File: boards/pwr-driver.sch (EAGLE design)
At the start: 32 parts

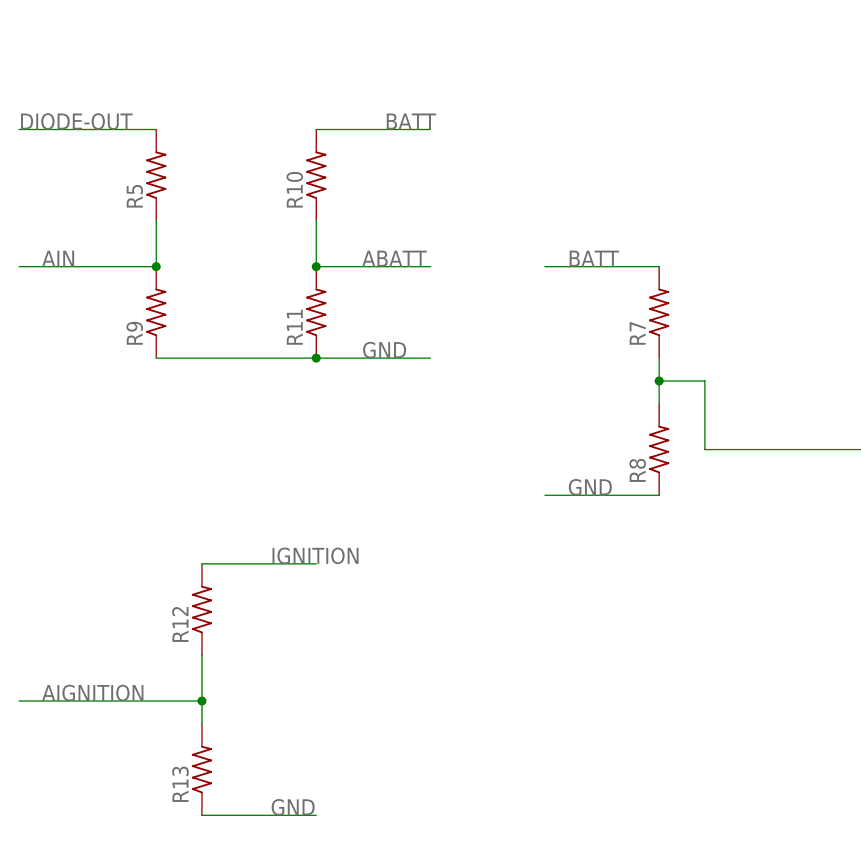
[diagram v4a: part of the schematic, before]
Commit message: Added resistor values to all of the resistor dividors.
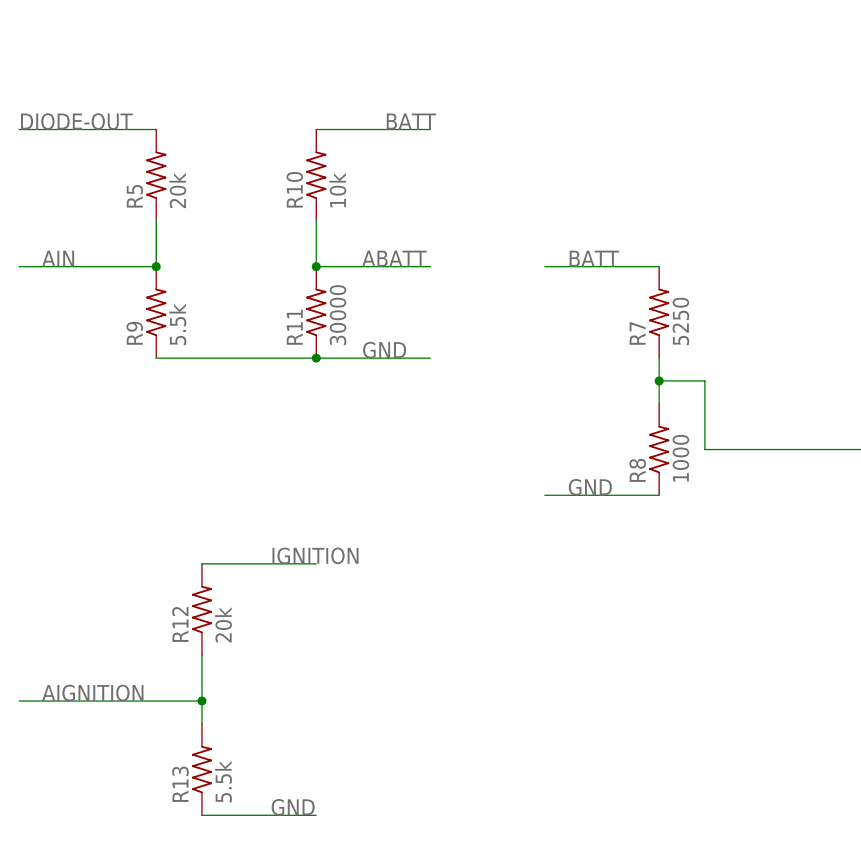
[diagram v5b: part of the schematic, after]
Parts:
- R10: value (none) -> 10k
- R11: value (none) -> 30000
- R12, R5: value (none) -> 20k
- R13, R9: value (none) -> 5.5k
- R7: value (none) -> 5250
- R8: value (none) -> 1000
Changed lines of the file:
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@@
 <part name="C5" library="resistor" deviceset="C-US" device="C0603" value=".1uf"/>
 <part name="U$1" library="needed-parts" deviceset="MPM80" device=""/>
-<part name="R7" library="resistor" deviceset="R-US_" device="R0603"/>
-<part name="R8" library="resistor" deviceset="R-US_" device="R0603"/>
+<part name="R7" library="resistor" deviceset="R-US_" device="R0603" value="5250"/>
+<part name="R8" library="resistor" deviceset="R-US_" device="R0603" value="1000"/>
 <part name="U$3" library="needed-parts" deviceset="STEP-UP-FROM-AMAZON" device=""/>
 <part name="BATT" library="pinhead" deviceset="PINHD-1X2" device=""/>
@@
 <part name="U$8" library="needed-parts" deviceset="PTC" device=""/>
 <part name="U$10" library="needed-parts" deviceset="ADS1013" device=""/>
-<part name="R5" library="resistor" deviceset="R-US_" device="R0603"/>
-<part name="R9" library="resistor" deviceset="R-US_" device="R0603"/>
-<part name="R10" library="resistor" deviceset="R-US_" device="R0603"/>
-<part name="R11" library="resistor" deviceset="R-US_" device="R0603"/>
-<part name="R12" library="resistor" deviceset="R-US_" device="R0603"/>
-<part name="R13" library="resistor" deviceset="R-US_" device="R0603"/>
+<part name="R5" library="resistor" deviceset="R-US_" device="R0603" value="20k"/>
+<part name="R9" library="resistor" deviceset="R-US_" device="R0603" value="5.5k"/>
+<part name="R10" library="resistor" deviceset="R-US_" device="R0603" value="10k"/>
+<part name="R11" library="resistor" deviceset="R-US_" device="R0603" value="30000"/>
+<part name="R12" library="resistor" deviceset="R-US_" device="R0603" value="20k"/>
+<part name="R13" library="resistor" deviceset="R-US_" device="R0603" value="5.5k"/>
 <part name="C2" library="resistor" deviceset="C-US" device="C0603" value=".1uf"/>
 <part name="U$15" library="needed-parts" deviceset="DIODE-403" device=""/>

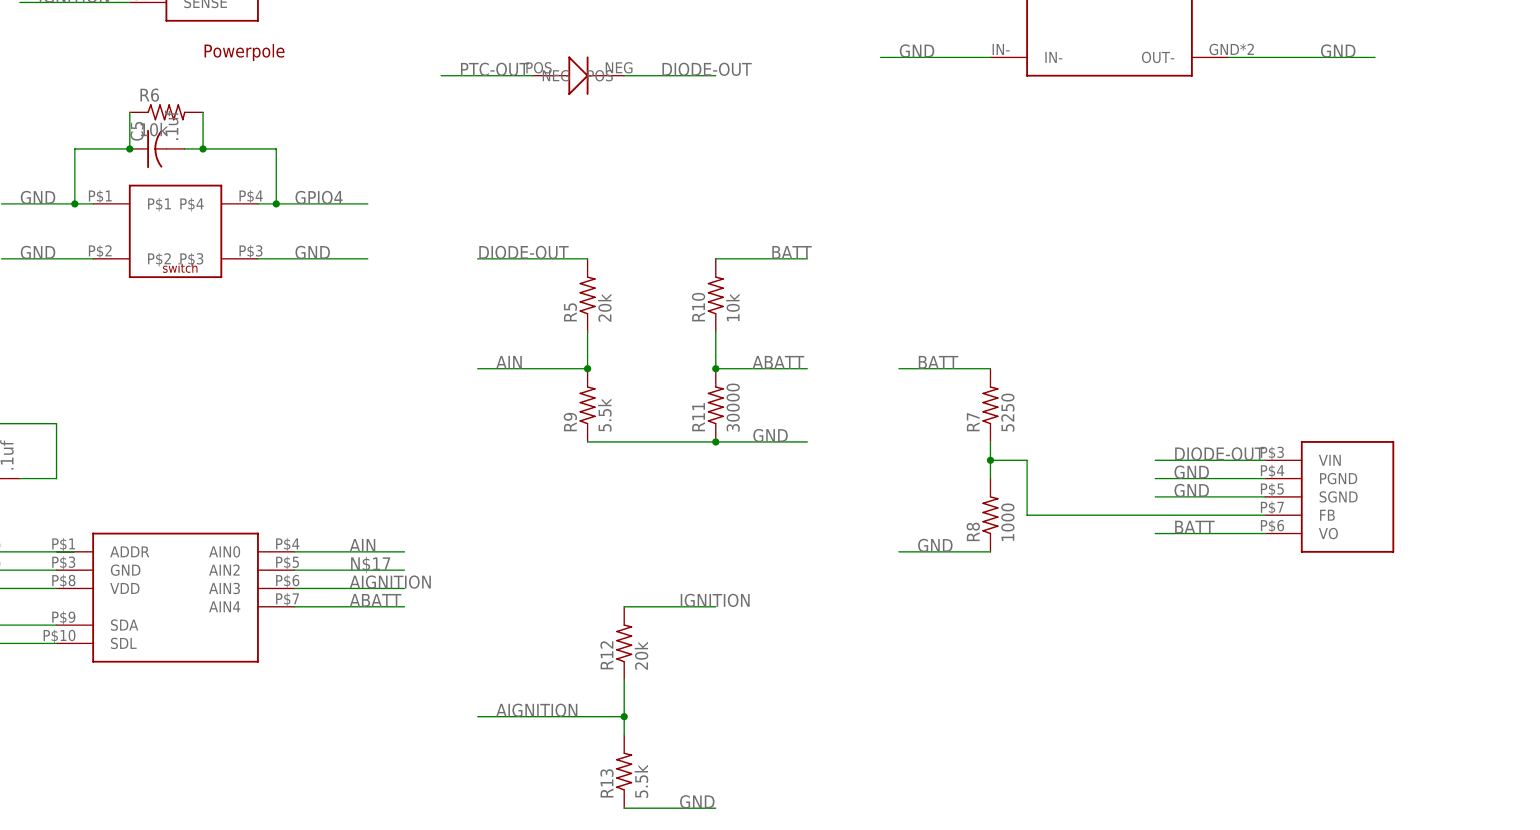
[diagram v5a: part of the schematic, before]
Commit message: dding description of Resistor dividors to schematic.
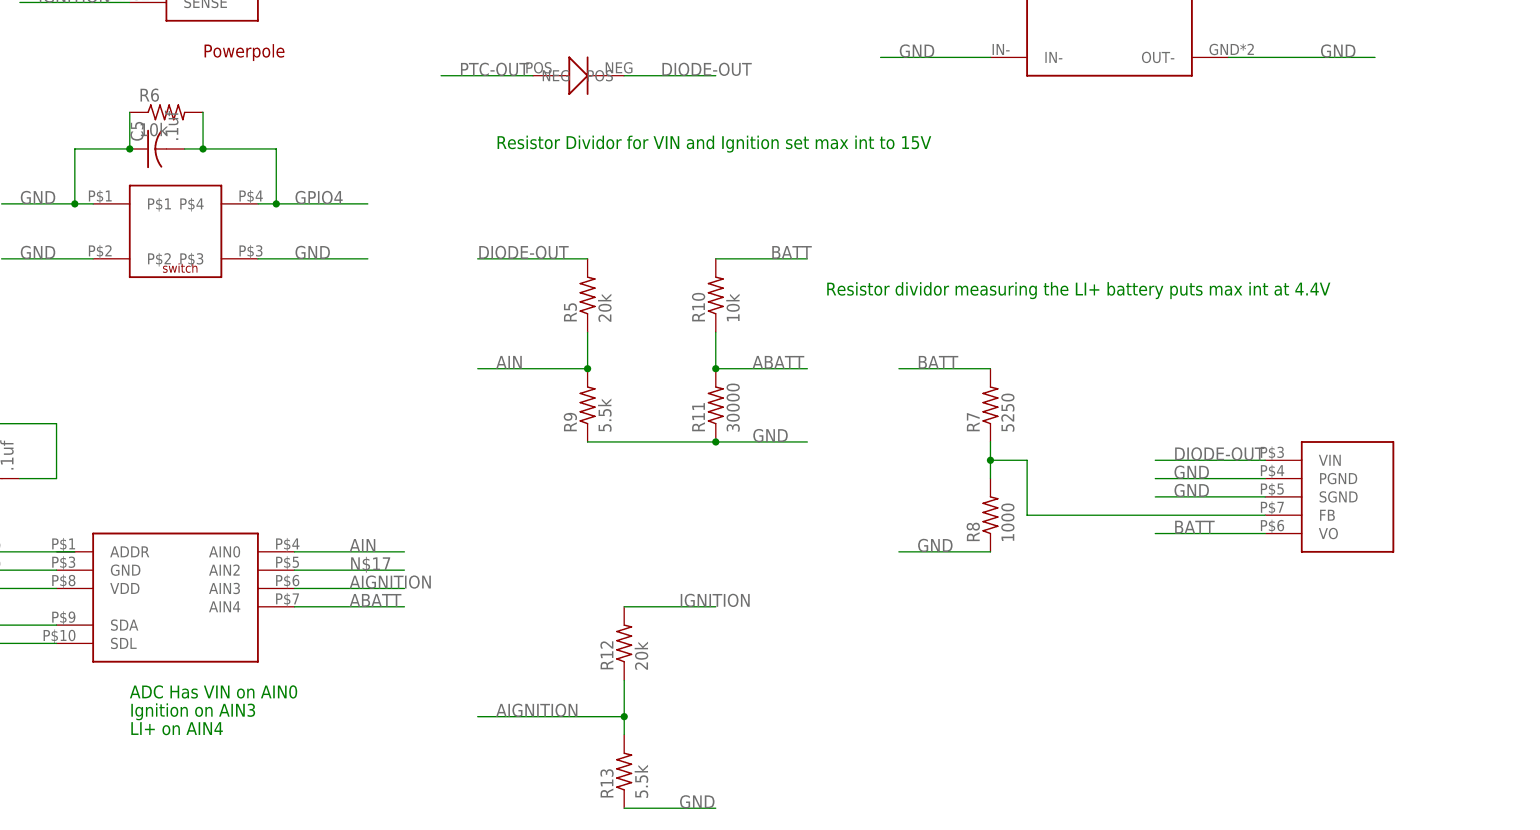
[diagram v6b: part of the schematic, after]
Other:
- note added: "ADC Has VIN on AIN0"
- note added: "Ignition on AIN3"
- note added: "LI+ on AIN4"
- note added: "Resistor Dividor for VIN and Ignition set max int to 15V"
- note added: "Resistor dividor measuring the LI+ battery puts max int at 4.4V"
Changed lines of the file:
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@@
 <text x="-10.16" y="48.26" size="1.778" layer="94">Vin cap</text>
 <text x="-60.96" y="27.94" size="1.778" layer="94">Powerpole</text>
+<text x="-20.32" y="15.24" size="1.778" layer="91">Resistor Dividor for VIN and Ignition set max int to 15V</text>
+<text x="25.4" y="-5.08" size="1.778" layer="91">Resistor dividor measuring the LI+ battery puts max int at 4.4V</text>
+<text x="-71.12" y="-60.96" size="1.778" layer="91">ADC Has VIN on AIN0</text>
+<text x="-71.12" y="-63.5" size="1.778" layer="91">Ignition on AIN3</text>
+<text x="-71.12" y="-66.04" size="1.778" layer="91">LI+ on AIN4</text>
 </plain>
 <instances>
